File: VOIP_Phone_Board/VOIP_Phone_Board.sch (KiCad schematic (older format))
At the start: 5 parts, among them P1 Conn_02x20_Odd_Even

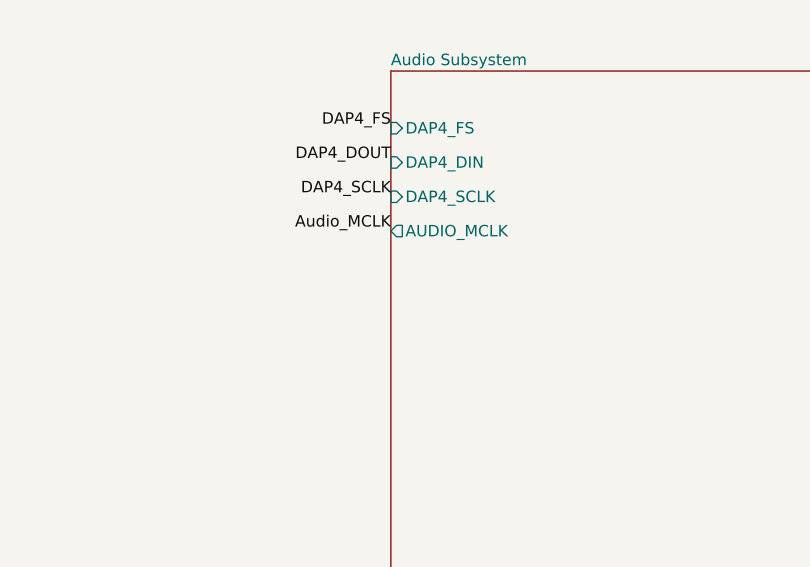
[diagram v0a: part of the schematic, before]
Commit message: Completed audio input section.
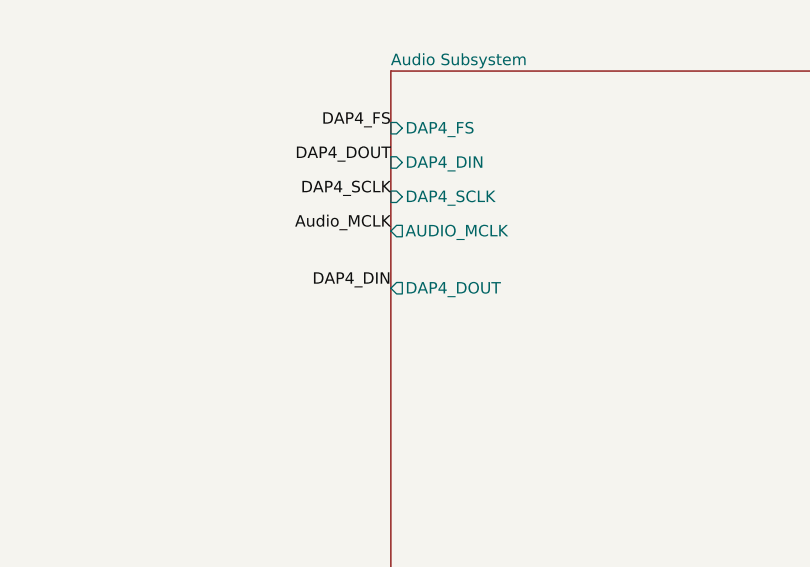
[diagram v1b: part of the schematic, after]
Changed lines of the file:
@@
 F4 "DAP4_SCLK" I L 6600 2150 50
 F5 "AUDIO_MCLK" O L 6600 2300 50
+F6 "DAP4_DOUT" O L 6600 2550 50
 $EndSheet
 $Sheet
@@
 Text Label 6600 2300 2    50   ~ 0
 Audio_MCLK
+Text Label 6600 2550 2    50   ~ 0
+DAP4_DIN
 $EndSCHEMATC

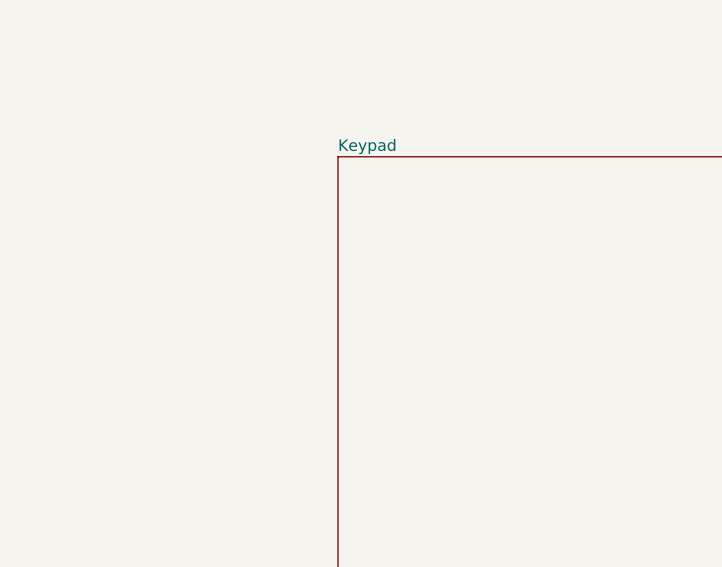
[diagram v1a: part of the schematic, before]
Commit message: Add keypad.
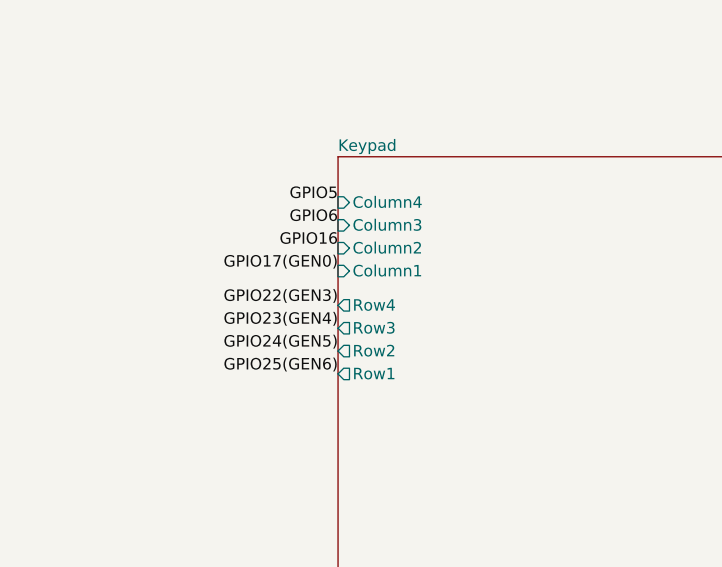
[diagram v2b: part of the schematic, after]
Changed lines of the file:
@@
 F0 "Keypad" 50
 F1 "Keypad.sch" 50
+F2 "Column4" I L 2050 4400 50
+F3 "Column3" I L 2050 4500 50
+F4 "Column2" I L 2050 4600 50
+F5 "Column1" I L 2050 4700 50
+F6 "Row4" O L 2050 4850 50
+F7 "Row3" O L 2050 4950 50
+F8 "Row2" O L 2050 5050 50
+F9 "Row1" O L 2050 5150 50
 $EndSheet
 $Sheet
@@
 Text Label 6600 2550 2    50   ~ 0
 DAP4_DIN
+Text Label 2050 4400 2    50   ~ 0
+GPIO5
+Text Label 2050 4500 2    50   ~ 0
+GPIO6
+Text Label 2050 4600 2    50   ~ 0
+GPIO16
+Text Label 2050 4700 2    50   ~ 0
+GPIO17(GEN0)
+Text Label 2050 4850 2    50   ~ 0
+GPIO22(GEN3)
+Text Label 2050 4950 2    50   ~ 0
+GPIO23(GEN4)
+Text Label 2050 5050 2    50   ~ 0
+GPIO24(GEN5)
+Text Label 2050 5150 2    50   ~ 0
+GPIO25(GEN6)
 $EndSCHEMATC

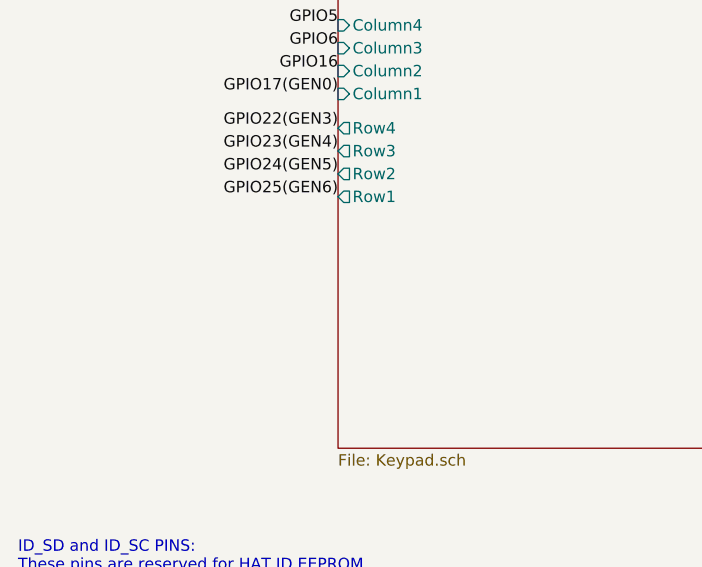
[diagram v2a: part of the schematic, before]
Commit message: Add Hook Switch.
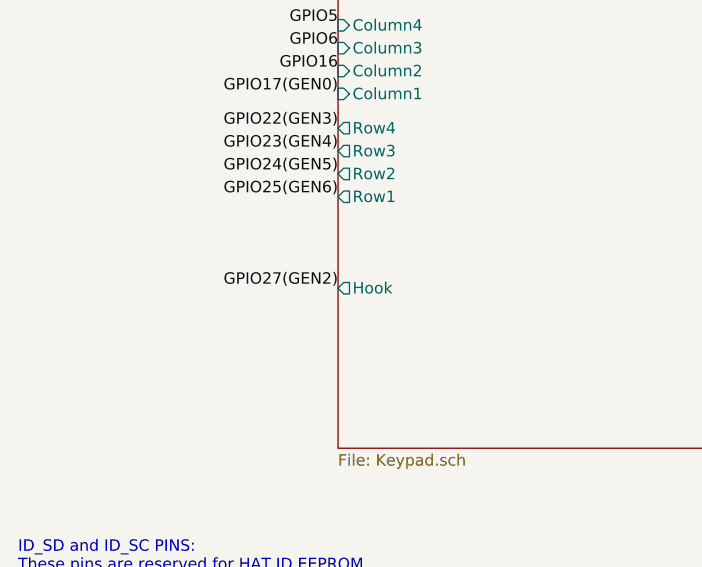
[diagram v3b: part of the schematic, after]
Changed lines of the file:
@@
 F8 "Row2" O L 2050 5050 50
 F9 "Row1" O L 2050 5150 50
+F10 "Hook" O L 2050 5550 50
 $EndSheet
 $Sheet
@@
 Text Label 2050 5150 2    50   ~ 0
 GPIO25(GEN6)
+Text Label 2050 5550 2    50   ~ 0
+GPIO27(GEN2)
 $EndSCHEMATC

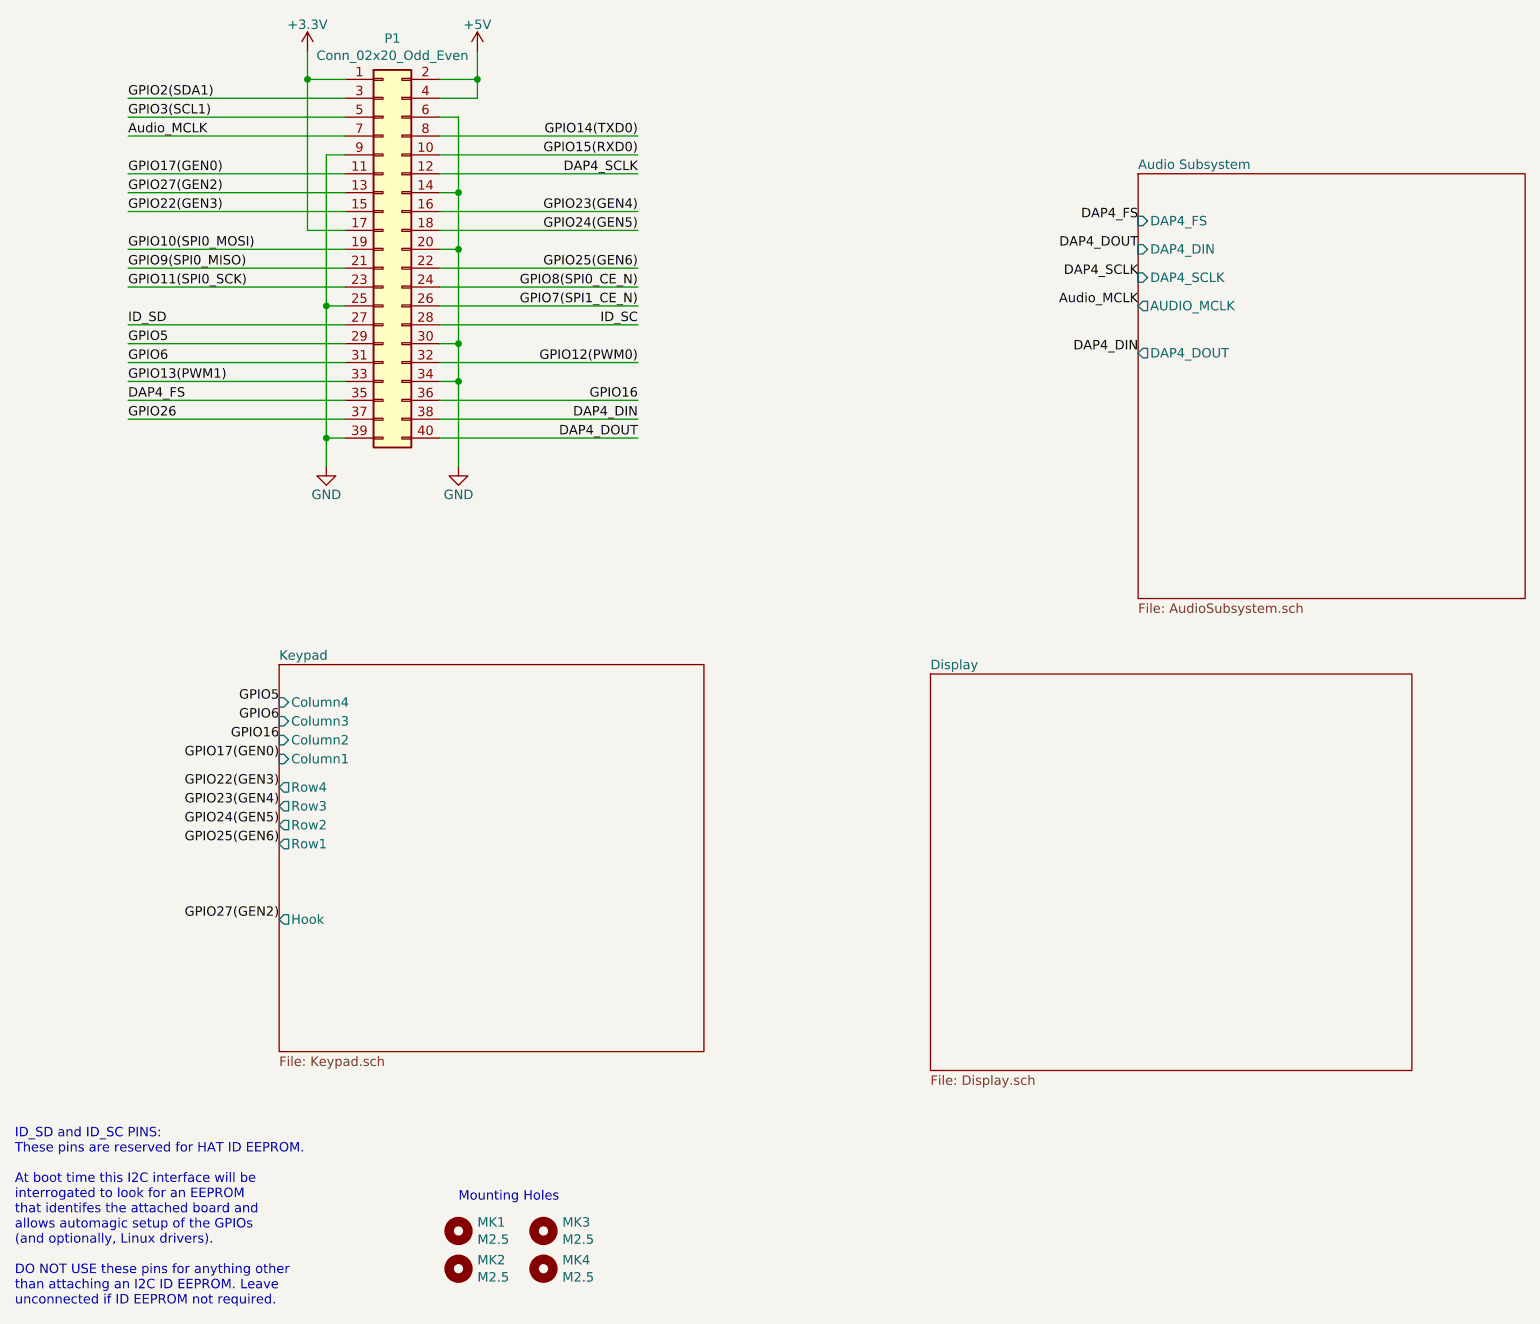
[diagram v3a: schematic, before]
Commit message: Complete all I/O and connectors.
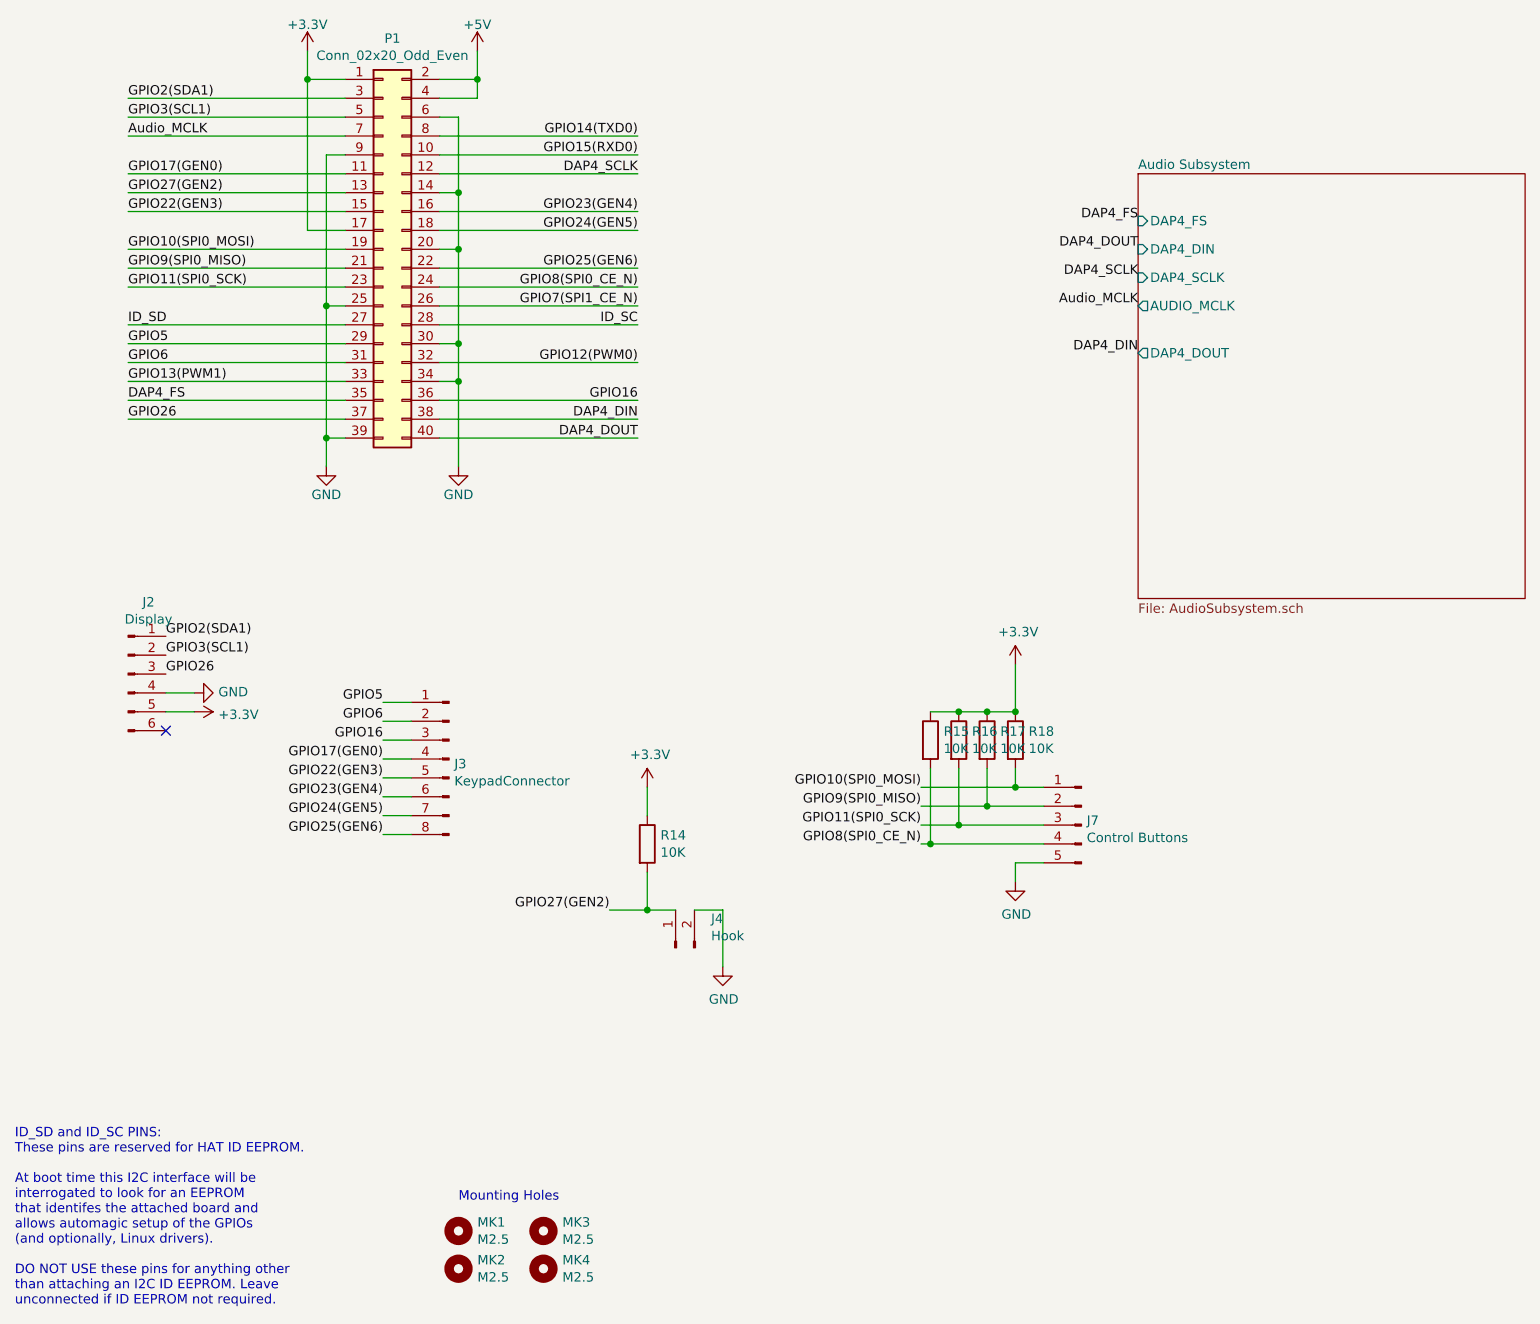
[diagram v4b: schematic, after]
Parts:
- added J2: Display, Connector_PinHeader_2.54mm:PinHeader_1x06_P2.54mm_Vertical, symbol Connector:Conn_01x06_Male
- added J3: KeypadConnector, Connector_PinHeader_2.54mm:PinHeader_1x08_P2.54mm_Vertical, symbol Keypad:KeypadConnector
- added J4: Hook, Connector_PinHeader_2.54mm:PinHeader_1x02_P2.54mm_Vertical, symbol Connector:Conn_01x02_Male
- added J7: Control Buttons, Connector_PinHeader_2.54mm:PinHeader_1x05_P2.54mm_Vertical, symbol Connector:Conn_01x05_Male
- added R14, R15, R16, R17, R18: 10K, Resistor_SMD:R_0603_1608Metric_Pad1.05x0.95mm_HandSolder, symbol Device:R
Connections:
- net +3V3: now also J2.5 (Pin_5), R14.1, R15.1, R16.1, R17.1, R18.1
- net GND: now also J2.4 (Pin_4), J4.2 (Pin_2), J7.5 (Pin_5)
- net GPIO10(SPI0_MOSI): now also J7.1 (Pin_1), R18.2
- net GPIO11(SPI0_SCK): now also J7.3 (Pin_3), R16.2
- net GPIO16: now also J3.3 (Column_2)
- net GPIO17(GEN0): now also J3.4 (Column_1)
- net GPIO2(SDA1): now also J2.1 (Pin_1)
- net GPIO22(GEN3): now also J3.5 (Row_4)
- net GPIO23(GEN4): now also J3.6 (Row_3)
- net GPIO24(GEN5): now also J3.7 (Row_2)
- net GPIO25(GEN6): now also J3.8 (Row_1)
- net GPIO26: now also J2.3 (Pin_3)
- net GPIO27(GEN2): now also J4.1 (Pin_1), R14.2
- net GPIO3(SCL1): now also J2.2 (Pin_2)
- net GPIO5: now also J3.1 (Column_4)
- net GPIO6: now also J3.2 (Column_3)
- net GPIO8(SPI0_CE_N): now also J7.4 (Pin_4), R15.2
- net GPIO9(SPI0_MISO): now also J7.2 (Pin_2), R17.2
- no-connect marks 0 -> 1

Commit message: MAX98357A Version.
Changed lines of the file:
@@
 F5 "AUDIO_MCLK" O L 6600 2300 50
 F6 "DAP4_DOUT" O L 6600 2550 50
+F7 "SpeakerEnable" I L 6600 2800 50
+F8 "HeadsetEnable" I L 6600 3100 50
 $EndSheet
 Text Label 6600 1850 2    50   ~ 0
@@
 Text Label 5450 5150 2    50   ~ 0
 GPIO8(SPI0_CE_N)
+Text Label 6600 2800 2    50   ~ 0
+GPIO12(PWM0)
+Text Label 6600 3100 2    50   ~ 0
+GPIO13(PWM1)
 $EndSCHEMATC

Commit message: Started with ADAU1361.
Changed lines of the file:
@@
 F5 "AUDIO_MCLK" O L 6600 2300 50
 F6 "DAP4_DOUT" O L 6600 2550 50
-F7 "SpeakerEnable" I L 6600 2800 50
-F8 "HeadsetEnable" I L 6600 3100 50
 $EndSheet
 Text Label 6600 1850 2    50   ~ 0
@@
 Text Label 5450 5150 2    50   ~ 0
 GPIO8(SPI0_CE_N)
-Text Label 6600 2800 2    50   ~ 0
-GPIO12(PWM0)
-Text Label 6600 3100 2    50   ~ 0
-GPIO13(PWM1)
 $EndSCHEMATC
